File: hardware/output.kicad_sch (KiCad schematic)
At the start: 10 parts, among them K1 FINDER-30.22, Q2 BSS123, Q3 BSS123

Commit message: full 3d models, pre-routing, corrections
kurwa bezpiecznik od wczoraj a fura dalej nie jeździ siedze u rakietowcow bo cieplo chlopaki co z wami
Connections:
- net +24V is gone; now on net VALVE_SUPPLY: K1.24
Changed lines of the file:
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@@
   (junction (at 116.84 102.87) (diameter 0) (color 0 0 0 0)
+  )
+  (junction (at 179.07 38.1) (diameter 0) (color 0 0 0 0)
   )
   (junction (at 166.37 49.53) (diameter 0) (color 0 0 0 0)
@@
     (stroke (width 0) (type default) (color 0 0 0 0))
   )
+  (wire (pts (xy 179.07 38.1) (xy 189.23 38.1))
+    (stroke (width 0) (type default) (color 0 0 0 0))
+  )
   (wire (pts (xy 101.6 138.43) (xy 101.6 139.7))
     (stroke (width 0) (type default) (color 0 0 0 0))
@@
     (stroke (width 0) (type default) (color 0 0 0 0))
   )
-  (wire (pts (xy 179.07 31.75) (xy 179.07 52.07))
+  (wire (pts (xy 179.07 31.75) (xy 179.07 38.1))
     (stroke (width 0) (type default) (color 0 0 0 0))
   )
@@
     (stroke (width 0) (type default) (color 0 0 0 0))
   )
+  (wire (pts (xy 179.07 38.1) (xy 179.07 52.07))
+    (stroke (width 0) (type default) (color 0 0 0 0))
+  )
   (wire (pts (xy 81.28 127) (xy 86.36 127))
     (stroke (width 0) (type default) (color 0 0 0 0))
@@
     (stroke (width 0) (type default) (color 0 0 0 0))
   )
-  (wire (pts (xy 189.23 29.21) (xy 189.23 52.07))
+  (wire (pts (xy 189.23 38.1) (xy 189.23 52.07))
     (stroke (width 0) (type default) (color 0 0 0 0))
   )
@@
     (pin "2")
   )
-  (symbol (lib_id "power:+24V") (at 189.23 29.21 0) (unit 1)
-    (in_bom yes) (on_board yes) (fields_autoplaced)
-    (property "Reference" "#PWR01" (id 0) (at 189.23 33.02 0)
-      (effects (font (size 1.27 1.27)) hide)
-    )
-    (property "Value" "+24V" (id 1) (at 189.23 24.13 0))
-    (property "Footprint" "" (id 2) (at 189.23 29.21 0)
-      (effects (font (size 1.27 1.27)) hide)
-    )
-    (property "Datasheet" "" (id 3) (at 189.23 29.21 0)
-      (effects (font (size 1.27 1.27)) hide)
-    )
-    (pin "1")
-  )
   (symbol (lib_id "Relay:FINDER-30.22") (at 176.53 59.69 0) (unit 1)

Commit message: WIP revision 2 layout refinement
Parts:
- D3, D4, D5: symbol Diode:1N5408 -> Diode:1N5817
- R14, R16: value 1k -> 100R
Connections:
- net AIR+ renamed TSMS
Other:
- note added: "//parallel to the AIR's"
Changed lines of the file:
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@@
+    (effects (font (size 1.27 1.27)) (justify left bottom))
+  )
+  (text "//parallel to the AIR's" (at 123.19 50.8 0)
     (effects (font (size 1.27 1.27)) (justify left bottom))
   )
@@
     )
   )
-  (global_label "AIR+" (shape input) (at 135.89 45.72 180) (fields_autoplaced)
+  (global_label "TSMS" (shape input) (at 135.89 45.72 180) (fields_autoplaced)
     (effects (font (size 1.27 1.27)) (justify right))
-    (property "Intersheetrefs" "${INTERSHEET_REFS}" (at 128.9412 45.6406 0)
+    (property "Intersheetrefs" "${INTERSHEET_REFS}" (at 128.1462 45.72 0)
       (effects (font (size 1.27 1.27)) (justify right) hide)
     )
@@
     )
   )
-  (symbol (lib_id "Diode:1N5408") (at 219.71 110.49 270) (unit 1)
+  (symbol (lib_id "Diode:1N5817") (at 219.71 110.49 270) (unit 1)
     (in_bom yes) (on_board yes) (dnp no) (fields_autoplaced)
     (property "Reference" "D5" (at 222.25 109.2199 90)
@@
     )
   )
-  (symbol (lib_id "Diode:1N5408") (at 151.13 60.96 270) (unit 1)
+  (symbol (lib_id "Diode:1N5817") (at 151.13 60.96 270) (unit 1)
     (in_bom yes) (on_board yes) (dnp no) (fields_autoplaced)
     (property "Reference" "D4" (at 153.67 59.6899 90)
@@
       (effects (font (size 1.27 1.27)))
     )
-    (property "Value" "1k" (at 208.28 132.08 90)
+    (property "Value" "100R" (at 208.28 132.08 90)
       (effects (font (size 1.27 1.27)))
     )
@@
       (effects (font (size 1.27 1.27)))
     )
-    (property "Value" "1k" (at 90.17 130.81 90)
+    (property "Value" "100R" (at 90.17 130.81 90)
       (effects (font (size 1.27 1.27)))
     )
@@
     )
   )
-  (symbol (lib_id "Diode:1N5408") (at 100.33 109.22 270) (unit 1)
+  (symbol (lib_id "Diode:1N5817") (at 100.33 109.22 270) (unit 1)
     (in_bom yes) (on_board yes) (dnp no) (fields_autoplaced)
     (property "Reference" "D3" (at 102.87 107.9499 90)

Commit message: 2.0 layot wip , routing 3
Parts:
- D3, D4, D5: footprint Diode_SMD:D_SMA_Handsoldering -> Diode_SMD:D_SMA
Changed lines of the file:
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@@
       (effects (font (size 1.27 1.27)) (justify left))
     )
-    (property "Footprint" "Diode_SMD:D_SMA_Handsoldering" (at 215.265 110.49 0)
+    (property "Footprint" "Diode_SMD:D_SMA" (at 215.265 110.49 0)
       (effects (font (size 1.27 1.27)) hide)
     )
@@
       (effects (font (size 1.27 1.27)) (justify left))
     )
-    (property "Footprint" "Diode_SMD:D_SMA_Handsoldering" (at 146.685 60.96 0)
+    (property "Footprint" "Diode_SMD:D_SMA" (at 146.685 60.96 0)
       (effects (font (size 1.27 1.27)) hide)
     )
@@
       (effects (font (size 1.27 1.27)) (justify left))
     )
-    (property "Footprint" "Diode_SMD:D_SMA_Handsoldering" (at 95.885 109.22 0)
+    (property "Footprint" "Diode_SMD:D_SMA" (at 95.885 109.22 0)
       (effects (font (size 1.27 1.27)) hide)
     )

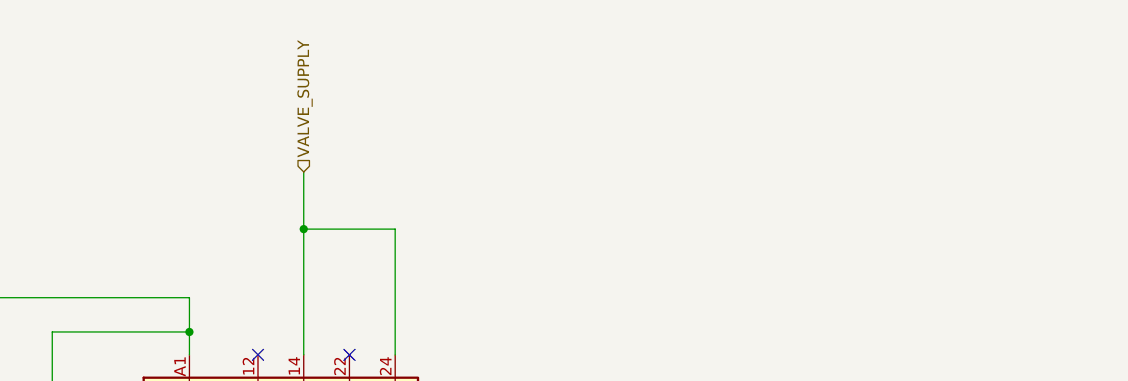
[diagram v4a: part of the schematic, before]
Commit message: replace RES2 input to actuator relai
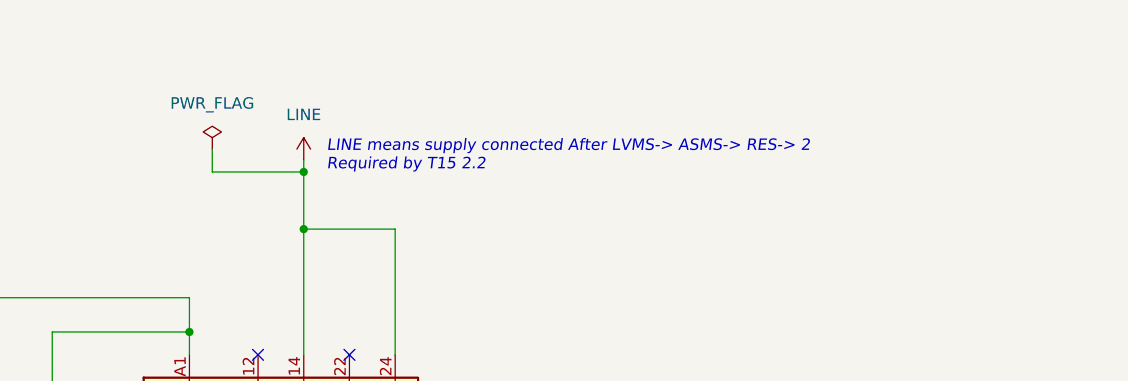
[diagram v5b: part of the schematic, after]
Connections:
- net VALVE_SUPPLY renamed LINE
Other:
- note added: "LINE means supply connected After LVMS-> ASMS-> RES-> 2 Required by T15 2.2"
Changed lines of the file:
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@@
   (junction (at 234.95 140.97) (diameter 0) (color 0 0 0 0)
   )
+  (junction (at 179.07 38.1) (diameter 0) (color 0 0 0 0)
+  )
   (junction (at 166.37 69.85) (diameter 0) (color 0 0 0 0)
   )
@@
   (junction (at 219.71 128.27) (diameter 0) (color 0 0 0 0)
   )
+  (junction (at 179.07 31.75) (diameter 0) (color 0 0 0 0)
+  )
   (junction (at 234.95 118.11) (diameter 0) (color 0 0 0 0)
   )
   (junction (at 116.84 102.87) (diameter 0) (color 0 0 0 0)
-  )
-  (junction (at 179.07 38.1) (diameter 0) (color 0 0 0 0)
   )
   (junction (at 166.37 49.53) (diameter 0) (color 0 0 0 0)
@@
   (no_connect (at 184.15 52.07))
   (no_connect (at 173.99 52.07))
+  (wire (pts (xy 179.07 31.75) (xy 179.07 38.1))
+    (stroke (width 0) (type default))
+  )
   (wire (pts (xy 219.71 118.11) (xy 234.95 118.11))
     (stroke (width 0) (type default))
@@
     (stroke (width 0) (type default))
   )
-  (wire (pts (xy 179.07 31.75) (xy 179.07 38.1))
-    (stroke (width 0) (type default))
-  )
   (wire (pts (xy 151.13 57.15) (xy 151.13 49.53))
     (stroke (width 0) (type default))
@@
     (stroke (width 0) (type default))
   )
+  (wire (pts (xy 81.28 127) (xy 86.36 127))
+    (stroke (width 0) (type default))
+  )
+  (wire (pts (xy 166.37 49.53) (xy 166.37 52.07))
+    (stroke (width 0) (type default))
+  )
+  (wire (pts (xy 179.07 30.48) (xy 179.07 31.75))
+    (stroke (width 0) (type default))
+  )
+  (wire (pts (xy 189.23 38.1) (xy 189.23 52.07))
+    (stroke (width 0) (type default))
+  )
+  (polyline (pts (xy 116.84 110.49) (xy 116.84 114.3))
+    (stroke (width 0) (type default))
+  )
+  (wire (pts (xy 130.81 73.66) (xy 166.37 73.66))
+    (stroke (width 0) (type default))
+  )
+  (wire (pts (xy 176.53 88.9) (xy 176.53 67.31))
+    (stroke (width 0) (type default))
+  )
+  (wire (pts (xy 179.07 31.75) (xy 168.91 31.75))
+    (stroke (width 0) (type default))
+  )
+  (wire (pts (xy 166.37 45.72) (xy 166.37 49.53))
+    (stroke (width 0) (type default))
+  )
+  (wire (pts (xy 196.85 128.27) (xy 204.47 128.27))
+    (stroke (width 0) (type default))
+  )
+  (polyline (pts (xy 238.76 107.95) (xy 231.14 107.95))
+    (stroke (width 0) (type default))
+  )
+  (polyline (pts (xy 120.65 110.49) (xy 120.65 105.41))
+    (stroke (width 0) (type default))
+  )
+  (polyline (pts (xy 231.14 113.03) (xy 238.76 113.03))
+    (stroke (width 0) (type default))
+  )
+  (wire (pts (xy 101.6 127) (xy 109.22 127))
+    (stroke (width 0) (type default))
+  )
+  (wire (pts (xy 135.89 45.72) (xy 166.37 45.72))
+    (stroke (width 0) (type default))
+  )
+  (wire (pts (xy 116.84 132.08) (xy 116.84 139.7))
+    (stroke (width 0) (type default))
+  )
+  (polyline (pts (xy 116.84 102.87) (xy 116.84 105.41))
+    (stroke (width 0) (type default))
+  )
+  (wire (pts (xy 130.81 76.2) (xy 130.81 73.66))
+    (stroke (width 0) (type default))
+  )
+  (polyline (pts (xy 113.03 105.41) (xy 120.65 110.49))
+    (stroke (width 0) (type default))
+  )
+  (wire (pts (xy 219.71 104.14) (xy 219.71 106.68))
+    (stroke (width 0) (type default))
+  )
+  (wire (pts (xy 151.13 64.77) (xy 151.13 69.85))
+    (stroke (width 0) (type default))
+  )
+  (polyline (pts (xy 113.03 105.41) (xy 113.03 110.49))
+    (stroke (width 0) (type default))
+  )
   (wire (pts (xy 179.07 38.1) (xy 179.07 52.07))
     (stroke (width 0) (type default))
   )
-  (wire (pts (xy 81.28 127) (xy 86.36 127))
-    (stroke (width 0) (type default))
-  )
-  (wire (pts (xy 166.37 49.53) (xy 166.37 52.07))
-    (stroke (width 0) (type default))
-  )
-  (wire (pts (xy 189.23 38.1) (xy 189.23 52.07))
-    (stroke (width 0) (type default))
-  )
-  (polyline (pts (xy 116.84 110.49) (xy 116.84 114.3))
-    (stroke (width 0) (type default))
-  )
-  (wire (pts (xy 130.81 73.66) (xy 166.37 73.66))
-    (stroke (width 0) (type default))
-  )
-  (wire (pts (xy 176.53 88.9) (xy 176.53 67.31))
-    (stroke (width 0) (type default))
-  )
-  (wire (pts (xy 166.37 45.72) (xy 166.37 49.53))
-    (stroke (width 0) (type default))
-  )
-  (wire (pts (xy 196.85 128.27) (xy 204.47 128.27))
-    (stroke (width 0) (type default))
-  )
-  (polyline (pts (xy 238.76 107.95) (xy 231.14 107.95))
-    (stroke (width 0) (type default))
-  )
-  (polyline (pts (xy 120.65 110.49) (xy 120.65 105.41))
-    (stroke (width 0) (type default))
-  )
-  (polyline (pts (xy 231.14 113.03) (xy 238.76 113.03))
-    (stroke (width 0) (type default))
-  )
-  (wire (pts (xy 101.6 127) (xy 109.22 127))
-    (stroke (width 0) (type default))
-  )
-  (wire (pts (xy 135.89 45.72) (xy 166.37 45.72))
-    (stroke (width 0) (type default))
-  )
-  (wire (pts (xy 116.84 132.08) (xy 116.84 139.7))
-    (stroke (width 0) (type default))
-  )
-  (polyline (pts (xy 116.84 102.87) (xy 116.84 105.41))
-    (stroke (width 0) (type default))
-  )
-  (wire (pts (xy 130.81 76.2) (xy 130.81 73.66))
-    (stroke (width 0) (type default))
-  )
-  (polyline (pts (xy 113.03 105.41) (xy 120.65 110.49))
-    (stroke (width 0) (type default))
-  )
-  (wire (pts (xy 219.71 104.14) (xy 219.71 106.68))
-    (stroke (width 0) (type default))
-  )
-  (wire (pts (xy 151.13 64.77) (xy 151.13 69.85))
-    (stroke (width 0) (type default))
-  )
-  (polyline (pts (xy 113.03 105.41) (xy 113.03 110.49))
-    (stroke (width 0) (type default))
-  )
   (wire (pts (xy 116.84 102.87) (xy 100.33 102.87))
     (stroke (width 0) (type default))
   )
   (polyline (pts (xy 231.14 107.95) (xy 238.76 113.03))
+    (stroke (width 0) (type default))
+  )
+  (wire (pts (xy 168.91 31.75) (xy 168.91 29.21))
     (stroke (width 0) (type default))
   )
@@
   (text "fundamental EBS actuator\n" (at 78.74 119.38 0)
     (effects (font (size 1.27 1.27)) (justify left bottom))
+  )
+  (text "LINE means supply connected After LVMS-> ASMS-> RES-> 2\nRequired by T15 2.2"
+    (at 181.61 31.75 0)
+    (effects (font (size 1.27 1.27) italic) (justify left bottom))
   )
   (text "//parallel to the AIR's" (at 123.19 50.8 0)
@@
     (effects (font (size 1.27 1.27)) (justify right))
   )
-  (hierarchical_label "VALVE_SUPPLY" (shape input) (at 179.07 31.75 90) (fields_autoplaced)
-    (effects (font (size 1.27 1.27)) (justify left))
-  )
   (hierarchical_label "VALVE_2_SIG" (shape input) (at 196.85 128.27 180) (fields_autoplaced)
     (effects (font (size 1.27 1.27)) (justify right))
@@
         (path "/d921fbb5-521e-405d-bdec-f40195adfa1c/5ac2ed84-f067-458b-b606-2c46aae0c926"
           (reference "D4") (unit 1)
+        )
+      )
+    )
+  )
+  (symbol (lib_id "power:LINE") (at 179.07 30.48 0) (unit 1)
+    (in_bom yes) (on_board yes) (dnp no) (fields_autoplaced)
+    (property "Reference" "#PWR0107" (at 179.07 34.29 0)
+      (effects (font (size 1.27 1.27)) hide)
+    )
+    (property "Value" "LINE" (at 179.07 25.4 0)
+      (effects (font (size 1.27 1.27)))
+    )
+    (property "Footprint" "" (at 179.07 30.48 0)
+      (effects (font (size 1.27 1.27)) hide)
+    )
+    (property "Datasheet" "" (at 179.07 30.48 0)
+      (effects (font (size 1.27 1.27)) hide)
+    )
+    (pin "1")
+    (instances
+      (project "PUTM_DV_EBS_2023"
+        (path "/d921fbb5-521e-405d-bdec-f40195adfa1c/81567b80-5afb-49a2-8e1a-6e4e57e56b9d"
+          (reference "#PWR0107") (unit 1)
+        )
+        (path "/d921fbb5-521e-405d-bdec-f40195adfa1c/5ac2ed84-f067-458b-b606-2c46aae0c926"
+          (reference "#PWR086") (unit 1)
         )
       )
@@
         )
       )
+    )
+  )
+  (symbol (lib_id "power:PWR_FLAG") (at 168.91 29.21 0) (unit 1)
+    (in_bom yes) (on_board yes) (dnp no) (fields_autoplaced)
+    (property "Reference" "#FLG0101" (at 168.91 27.305 0)
+      (effects (font (size 1.27 1.27)) hide)
+    )
+    (property "Value" "PWR_FLAG" (at 168.91 24.13 0)
+      (effects (font (size 1.27 1.27)))
+    )
+    (property "Footprint" "" (at 168.91 29.21 0)
+      (effects (font (size 1.27 1.27)) hide)
+    )
+    (property "Datasheet" "~" (at 168.91 29.21 0)
+      (effects (font (size 1.27 1.27)) hide)
+    )
+    (pin "1")
+    (instances
+      (project "PUTM_DV_EBS_2023"
+        (path "/d921fbb5-521e-405d-bdec-f40195adfa1c/81567b80-5afb-49a2-8e1a-6e4e57e56b9d"
+          (reference "#FLG0101") (unit 1)
+        )
+        (path "/d921fbb5-521e-405d-bdec-f40195adfa1c/5ac2ed84-f067-458b-b606-2c46aae0c926"
+          (reference "#FLG04") (unit 1)
+        )
+      )

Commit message: changed pcb version
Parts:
- D3, D4, D5: footprint Diode_SMD:D_SMA -> Diode_SMD:D_SMA_Handsoldering; symbol Diode:1N5817 -> Diode:1N5408
- R14, R16: value 100R -> 1k
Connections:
- net LINE renamed VALVE_SUPPLY
- net TSMS renamed AIR+
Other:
- note removed: "//parallel to the AIR's"
- note removed: "LINE means supply connected After LVMS-> ASMS-> RES-> 2 Required by T15 2.2"
